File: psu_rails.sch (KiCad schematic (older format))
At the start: 16 parts, among them Q401 BC846BPN

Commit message: WIP: Assign footprints
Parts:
- C401, C402: footprint (none) -> Capacitor_SMD:C_1206_3216Metric_Pad1.42x1.75mm_HandSolder
- C403, C404: footprint (none) -> Capacitor_SMD:CP_Elec_8x10.5; Part number EEE1HA221UAP -> EEE1EA221UP
- C405, C406, C407, C408, C409: footprint (none) -> Capacitor_SMD:C_0603_1608Metric_Pad1.05x0.95mm_HandSolder
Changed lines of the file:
@@
 F 0 "C405" H 5300 3400 50  0000 L CNN
 F 1 "100n" H 5300 3300 50  0000 L CNN
-F 2 "" H 5388 2850 50  0001 C CNN
+F 2 "Capacitor_SMD:C_0603_1608Metric_Pad1.05x0.95mm_HandSolder" H 5388 2850 50  0001 C CNN
 F 3 "~" H 5350 3000 50  0001 C CNN
 F 4 "VJ0603Y104KXACW1BC" H 0   0   50  0001 C CNN "Part number"
@@
 F 0 "C407" H 5600 3400 50  0000 L CNN
 F 1 "100n" H 5600 3300 50  0000 L CNN
-F 2 "" H 5688 2850 50  0001 C CNN
+F 2 "Capacitor_SMD:C_0603_1608Metric_Pad1.05x0.95mm_HandSolder" H 5688 2850 50  0001 C CNN
 F 3 "~" H 5650 3000 50  0001 C CNN
 F 4 "VJ0603Y104KXACW1BC" H 0   0   50  0001 C CNN "Part number"
@@
 F 0 "C403" H 5000 3400 50  0000 L CNN
 F 1 "220u" H 4950 3300 50  0000 L CNN
-F 2 "" H 5088 2850 50  0001 C CNN
+F 2 "Capacitor_SMD:CP_Elec_8x10.5" H 5088 2850 50  0001 C CNN
 F 3 "~" H 5050 3000 50  0001 C CNN
-F 4 "EEE1HA221UAP" H 0   0   50  0001 C CNN "Part number"
+F 4 "EEE1EA221UP" H 0   0   50  0001 C CNN "Part number"
 F 5 "SMT Electrolytic 25V" H 0   0   50  0001 C CNN "Parameters"
 	1    5050 3000
@@
 AR Path="/5D8DB5B0/5D8DBE1B" Ref="#PWR0403"  Part="1"
 AR Path="/5D8E5F02/5D8DBE1B" Ref="#PWR0503"  Part="1"
-F 0 "#PWR0403" H 5050 2950 50  0001 C CNN
+F 0 "#PWR0503" H 5050 2950 50  0001 C CNN
 F 1 "GND" H 5055 3027 50  0000 C CNN
 F 2 "" H 5050 3200 50  0001 C CNN
@@
 AR Path="/5D8DB5B0/5D8DBE37" Ref="#PWR0405"  Part="1"
 AR Path="/5D8E5F02/5D8DBE37" Ref="#PWR0505"  Part="1"
-F 0 "#PWR0405" H 5350 2950 50  0001 C CNN
+F 0 "#PWR0505" H 5350 2950 50  0001 C CNN
 F 1 "GND" H 5355 3027 50  0000 C CNN
 F 2 "" H 5350 3200 50  0001 C CNN
@@
 AR Path="/5D8DB5B0/5D8DBE4C" Ref="#PWR0407"  Part="1"
 AR Path="/5D8E5F02/5D8DBE4C" Ref="#PWR0507"  Part="1"
-F 0 "#PWR0407" H 5650 2950 50  0001 C CNN
+F 0 "#PWR0507" H 5650 2950 50  0001 C CNN
 F 1 "GND" H 5655 3027 50  0000 C CNN
 F 2 "" H 5650 3200 50  0001 C CNN
@@
 AR Path="/5D8DB5B0/5D8DBF9B" Ref="#PWR0404"  Part="1"
 AR Path="/5D8E5F02/5D8DBF9B" Ref="#PWR0504"  Part="1"
-F 0 "#PWR0404" H 5050 4800 50  0001 C CNN
+F 0 "#PWR0504" H 5050 4800 50  0001 C CNN
 F 1 "GND" H 5055 4877 50  0000 C CNN
 F 2 "" H 5050 5050 50  0001 C CNN
@@
 AR Path="/5D8DB5B0/5D8DBFA1" Ref="#PWR0406"  Part="1"
 AR Path="/5D8E5F02/5D8DBFA1" Ref="#PWR0506"  Part="1"
-F 0 "#PWR0406" H 5350 4800 50  0001 C CNN
+F 0 "#PWR0506" H 5350 4800 50  0001 C CNN
 F 1 "GND" H 5355 4877 50  0000 C CNN
 F 2 "" H 5350 5050 50  0001 C CNN
@@
 AR Path="/5D8DB5B0/5D8DBFA7" Ref="#PWR0408"  Part="1"
 AR Path="/5D8E5F02/5D8DBFA7" Ref="#PWR0508"  Part="1"
-F 0 "#PWR0408" H 5650 4800 50  0001 C CNN
+F 0 "#PWR0508" H 5650 4800 50  0001 C CNN
 F 1 "GND" H 5655 4877 50  0000 C CNN
 F 2 "" H 5650 5050 50  0001 C CNN
@@
 F 0 "C409" H 6365 3796 50  0000 L CNN
 F 1 "100n" H 6365 3705 50  0000 L CNN
-F 2 "" H 6288 3600 50  0001 C CNN
+F 2 "Capacitor_SMD:C_0603_1608Metric_Pad1.05x0.95mm_HandSolder" H 6288 3600 50  0001 C CNN
 F 3 "~" H 6250 3750 50  0001 C CNN
 F 4 "VJ0603Y104KXACW1BC" H 0   0   50  0001 C CNN "Part number"
@@
 F 0 "C406" H 5300 5250 50  0000 L CNN
 F 1 "100n" H 5300 5150 50  0000 L CNN
-F 2 "" H 5388 4700 50  0001 C CNN
+F 2 "Capacitor_SMD:C_0603_1608Metric_Pad1.05x0.95mm_HandSolder" H 5388 4700 50  0001 C CNN
 F 3 "~" H 5350 4850 50  0001 C CNN
 F 4 "VJ0603Y104KXACW1BC" H 0   0   50  0001 C CNN "Part number"
@@
 F 0 "C408" H 5600 5250 50  0000 L CNN
 F 1 "100n" H 5600 5150 50  0000 L CNN
-F 2 "" H 5688 4700 50  0001 C CNN
+F 2 "Capacitor_SMD:C_0603_1608Metric_Pad1.05x0.95mm_HandSolder" H 5688 4700 50  0001 C CNN
 F 3 "~" H 5650 4850 50  0001 C CNN
 F 4 "VJ0603Y104KXACW1BC" H 0   0   50  0001 C CNN "Part number"
@@
 F 0 "C404" H 5000 4450 50  0000 L CNN
 F 1 "220u" H 4950 4550 50  0000 L CNN
-F 2 "" H 5088 4700 50  0001 C CNN
+F 2 "Capacitor_SMD:CP_Elec_8x10.5" H 5088 4700 50  0001 C CNN
 F 3 "~" H 5050 4850 50  0001 C CNN
-F 4 "EEE1HA221UAP" H 0   0   50  0001 C CNN "Part number"
+F 4 "EEE1EA221UP" H 0   0   50  0001 C CNN "Part number"
 F 5 "SMT Electrolytic 25V" H 0   0   50  0001 C CNN "Parameters"
 	1    5050 4850
@@
 F 0 "C401" H 4618 3696 50  0000 L CNN
 F 1 "10u" H 4618 3605 50  0000 L CNN
-F 2 "" H 4538 3500 50  0001 C CNN
+F 2 "Capacitor_SMD:C_1206_3216Metric_Pad1.42x1.75mm_HandSolder" H 4538 3500 50  0001 C CNN
 F 3 "~" H 4500 3650 50  0001 C CNN
 F 4 "X7R/X5R 25V 1206" H 0   0   50  0001 C CNN "Parameters"
@@
 F 0 "C402" H 4382 5454 50  0000 R CNN
 F 1 "10u" H 4382 5545 50  0000 R CNN
-F 2 "" H 4538 5350 50  0001 C CNN
+F 2 "Capacitor_SMD:C_1206_3216Metric_Pad1.42x1.75mm_HandSolder" H 4538 5350 50  0001 C CNN
 F 3 "~" H 4500 5500 50  0001 C CNN
 F 4 "X7R/X5R 25V 1206" H 0   0   50  0001 C CNN "Parameters"
@@
 AR Path="/5D8DB5B0/5D8DF531" Ref="#PWR0401"  Part="1"
 AR Path="/5D8E5F02/5D8DF531" Ref="#PWR0501"  Part="1"
-F 0 "#PWR0401" H 4500 3600 50  0001 C CNN
+F 0 "#PWR0501" H 4500 3600 50  0001 C CNN
 F 1 "GND" H 4505 3677 50  0000 C CNN
 F 2 "" H 4500 3850 50  0001 C CNN
@@
 AR Path="/5D8DB5B0/5D8DF556" Ref="#PWR0402"  Part="1"
 AR Path="/5D8E5F02/5D8DF556" Ref="#PWR0502"  Part="1"
-F 0 "#PWR0402" H 4500 5450 50  0001 C CNN
+F 0 "#PWR0502" H 4500 5450 50  0001 C CNN
 F 1 "GND" H 4505 5527 50  0000 C CNN
 F 2 "" H 4500 5700 50  0001 C CNN

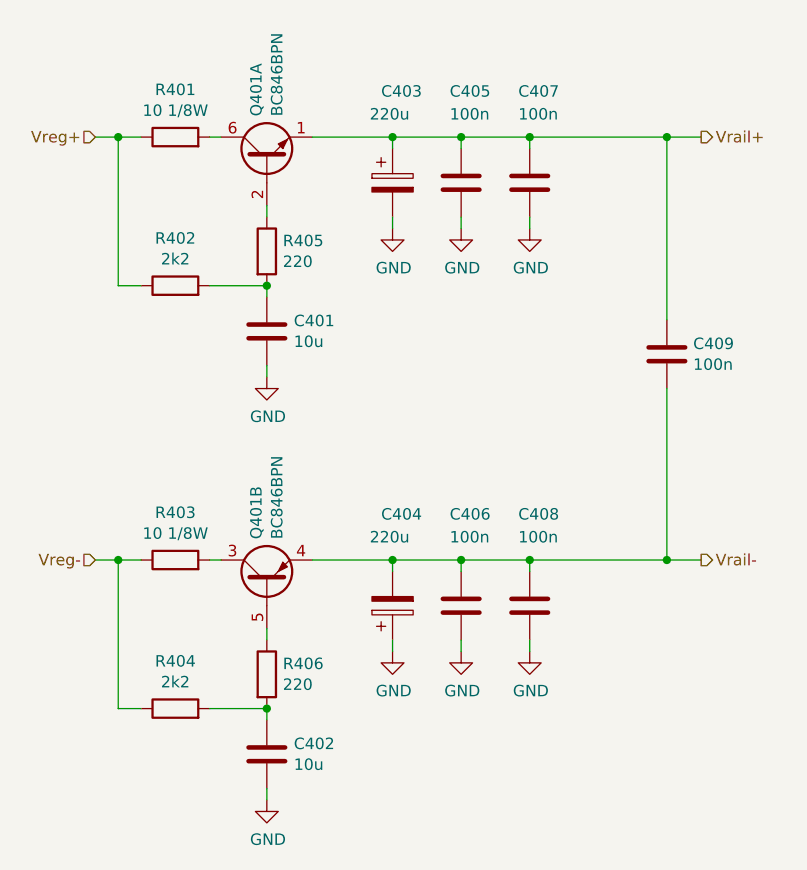
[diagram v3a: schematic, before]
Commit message: WIP: Assign footprints
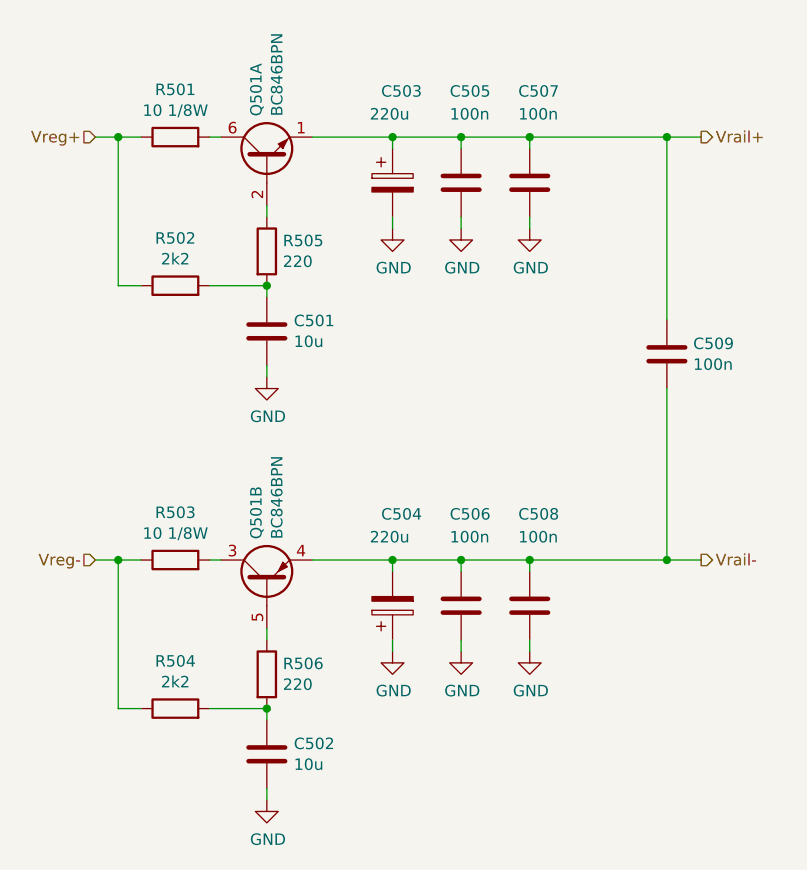
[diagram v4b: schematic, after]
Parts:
- R401, R403: footprint (none) -> Resistor_SMD:R_0805_2012Metric_Pad1.15x1.40mm_HandSolder
- R402, R404, R405, R406: footprint (none) -> Resistor_SMD:R_0603_1608Metric_Pad1.05x0.95mm_HandSolder
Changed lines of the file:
@@
 AR Path="/5D8DB5B0/5D8DB789" Ref="Q401"  Part="1"
 AR Path="/5D8E5F02/5D8DB789" Ref="Q501"  Part="1"
-F 0 "Q401" H 4691 2946 50  0000 L CNN
+F 0 "Q501" H 4691 2946 50  0000 L CNN
 F 1 "BC846BPN" H 4691 2855 50  0000 L CNN
 F 2 "Package_TO_SOT_SMD:SOT-363_SC-70-6" H 4700 3000 50  0001 C CNN
@@
 AR Path="/5D8DB5B0/5D8DB7C6" Ref="Q401"  Part="2"
 AR Path="/5D8E5F02/5D8DB7C6" Ref="Q501"  Part="2"
-F 0 "Q401" H 4691 4796 50  0000 L CNN
+F 0 "Q501" H 4691 4796 50  0000 L CNN
 F 1 "BC846BPN" H 4691 4705 50  0000 L CNN
 F 2 "Package_TO_SOT_SMD:SOT-363_SC-70-6" H 4700 4850 50  0001 C CNN
@@
 AR Path="/5D8DB5B0/5D8DBC14" Ref="C405"  Part="1"
 AR Path="/5D8E5F02/5D8DBC14" Ref="C505"  Part="1"
-F 0 "C405" H 5300 3400 50  0000 L CNN
+F 0 "C505" H 5300 3400 50  0000 L CNN
 F 1 "100n" H 5300 3300 50  0000 L CNN
 F 2 "Capacitor_SMD:C_0603_1608Metric_Pad1.05x0.95mm_HandSolder" H 5388 2850 50  0001 C CNN
@@
 AR Path="/5D8DB5B0/5D8DBC36" Ref="C407"  Part="1"
 AR Path="/5D8E5F02/5D8DBC36" Ref="C507"  Part="1"
-F 0 "C407" H 5600 3400 50  0000 L CNN
+F 0 "C507" H 5600 3400 50  0000 L CNN
 F 1 "100n" H 5600 3300 50  0000 L CNN
 F 2 "Capacitor_SMD:C_0603_1608Metric_Pad1.05x0.95mm_HandSolder" H 5688 2850 50  0001 C CNN
@@
 AR Path="/5D8DB5B0/5D8DBD04" Ref="C403"  Part="1"
 AR Path="/5D8E5F02/5D8DBD04" Ref="C503"  Part="1"
-F 0 "C403" H 5000 3400 50  0000 L CNN
+F 0 "C503" H 5000 3400 50  0000 L CNN
 F 1 "220u" H 4950 3300 50  0000 L CNN
 F 2 "Capacitor_SMD:CP_Elec_8x10.5" H 5088 2850 50  0001 C CNN
@@
 AR Path="/5D8DB5B0/5D8DC249" Ref="C409"  Part="1"
 AR Path="/5D8E5F02/5D8DC249" Ref="C509"  Part="1"
-F 0 "C409" H 6365 3796 50  0000 L CNN
+F 0 "C509" H 6365 3796 50  0000 L CNN
 F 1 "100n" H 6365 3705 50  0000 L CNN
 F 2 "Capacitor_SMD:C_0603_1608Metric_Pad1.05x0.95mm_HandSolder" H 6288 3600 50  0001 C CNN
@@
 AR Path="/5D8DB5B0/5D8DCC24" Ref="C406"  Part="1"
 AR Path="/5D8E5F02/5D8DCC24" Ref="C506"  Part="1"
-F 0 "C406" H 5300 5250 50  0000 L CNN
+F 0 "C506" H 5300 5250 50  0000 L CNN
 F 1 "100n" H 5300 5150 50  0000 L CNN
 F 2 "Capacitor_SMD:C_0603_1608Metric_Pad1.05x0.95mm_HandSolder" H 5388 4700 50  0001 C CNN
@@
 AR Path="/5D8DB5B0/5D8DCC2A" Ref="C408"  Part="1"
 AR Path="/5D8E5F02/5D8DCC2A" Ref="C508"  Part="1"
-F 0 "C408" H 5600 5250 50  0000 L CNN
+F 0 "C508" H 5600 5250 50  0000 L CNN
 F 1 "100n" H 5600 5150 50  0000 L CNN
 F 2 "Capacitor_SMD:C_0603_1608Metric_Pad1.05x0.95mm_HandSolder" H 5688 4700 50  0001 C CNN
@@
 AR Path="/5D8DB5B0/5D8DCC30" Ref="C404"  Part="1"
 AR Path="/5D8E5F02/5D8DCC30" Ref="C504"  Part="1"
-F 0 "C404" H 5000 4450 50  0000 L CNN
+F 0 "C504" H 5000 4450 50  0000 L CNN
 F 1 "220u" H 4950 4550 50  0000 L CNN
 F 2 "Capacitor_SMD:CP_Elec_8x10.5" H 5088 4700 50  0001 C CNN
@@
 AR Path="/5D8DB5B0/5D8DDC3C" Ref="C401"  Part="1"
 AR Path="/5D8E5F02/5D8DDC3C" Ref="C501"  Part="1"
-F 0 "C401" H 4618 3696 50  0000 L CNN
+F 0 "C501" H 4618 3696 50  0000 L CNN
 F 1 "10u" H 4618 3605 50  0000 L CNN
 F 2 "Capacitor_SMD:C_1206_3216Metric_Pad1.42x1.75mm_HandSolder" H 4538 3500 50  0001 C CNN
@@
 AR Path="/5D8DB5B0/5D8DE233" Ref="C402"  Part="1"
 AR Path="/5D8E5F02/5D8DE233" Ref="C502"  Part="1"
-F 0 "C402" H 4382 5454 50  0000 R CNN
+F 0 "C502" H 4382 5454 50  0000 R CNN
 F 1 "10u" H 4382 5545 50  0000 R CNN
 F 2 "Capacitor_SMD:C_1206_3216Metric_Pad1.42x1.75mm_HandSolder" H 4538 5350 50  0001 C CNN
@@
 AR Path="/5D8DB5B0/5D8DF470" Ref="R405"  Part="1"
 AR Path="/5D8E5F02/5D8DF470" Ref="R505"  Part="1"
-F 0 "R405" H 4570 3346 50  0000 L CNN
+F 0 "R505" H 4570 3346 50  0000 L CNN
 F 1 "220" H 4570 3255 50  0000 L CNN
-F 2 "" V 4430 3300 50  0001 C CNN
+F 2 "Resistor_SMD:R_0603_1608Metric_Pad1.05x0.95mm_HandSolder" V 4430 3300 50  0001 C CNN
 F 3 "~" H 4500 3300 50  0001 C CNN
 F 4 "ERA3AEB221V" H 0   0   50  0001 C CNN "Part number"
@@
 AR Path="/5D8DB5B0/5D8DF4B2" Ref="R406"  Part="1"
 AR Path="/5D8E5F02/5D8DF4B2" Ref="R506"  Part="1"
-F 0 "R406" H 4570 5196 50  0000 L CNN
+F 0 "R506" H 4570 5196 50  0000 L CNN
 F 1 "220" H 4570 5105 50  0000 L CNN
-F 2 "" V 4430 5150 50  0001 C CNN
+F 2 "Resistor_SMD:R_0603_1608Metric_Pad1.05x0.95mm_HandSolder" V 4430 5150 50  0001 C CNN
 F 3 "~" H 4500 5150 50  0001 C CNN
 F 4 "ERA3AEB221V" H 0   0   50  0001 C CNN "Part number"
@@
 AR Path="/5D8DB5B0/5D8E16D4" Ref="R401"  Part="1"
 AR Path="/5D8E5F02/5D8E16D4" Ref="R501"  Part="1"
-F 0 "R401" V 4307 2800 50  0000 C CNN
+F 0 "R501" V 4307 2800 50  0000 C CNN
 F 1 "10 1/8W" V 4216 2800 50  0000 C CNN
-F 2 "" V 4030 2800 50  0001 C CNN
+F 2 "Resistor_SMD:R_0805_2012Metric_Pad1.15x1.40mm_HandSolder" V 4030 2800 50  0001 C CNN
 F 3 "~" H 4100 2800 50  0001 C CNN
 F 4 "MCWF08U10RBTL" H 0   0   50  0001 C CNN "Part number"
@@
 AR Path="/5D8DB5B0/5D8E1F53" Ref="R402"  Part="1"
 AR Path="/5D8E5F02/5D8E1F53" Ref="R502"  Part="1"
-F 0 "R402" V 4307 3450 50  0000 C CNN
+F 0 "R502" V 4307 3450 50  0000 C CNN
 F 1 "2k2" V 4216 3450 50  0000 C CNN
-F 2 "" V 4030 3450 50  0001 C CNN
+F 2 "Resistor_SMD:R_0603_1608Metric_Pad1.05x0.95mm_HandSolder" V 4030 3450 50  0001 C CNN
 F 3 "~" H 4100 3450 50  0001 C CNN
 F 4 "RT0603FRE072K2L" H 0   0   50  0001 C CNN "Part number"
@@
 AR Path="/5D8DB5B0/5D8E1F97" Ref="R403"  Part="1"
 AR Path="/5D8E5F02/5D8E1F97" Ref="R503"  Part="1"
-F 0 "R403" V 4307 4650 50  0000 C CNN
+F 0 "R503" V 4307 4650 50  0000 C CNN
 F 1 "10 1/8W" V 4216 4650 50  0000 C CNN
-F 2 "" V 4030 4650 50  0001 C CNN
+F 2 "Resistor_SMD:R_0805_2012Metric_Pad1.15x1.40mm_HandSolder" V 4030 4650 50  0001 C CNN
 F 3 "~" H 4100 4650 50  0001 C CNN
 F 4 "MCWF08U10RBTL" H 0   0   50  0001 C CNN "Part number"
@@
 AR Path="/5D8DB5B0/5D8E1FEF" Ref="R404"  Part="1"
 AR Path="/5D8E5F02/5D8E1FEF" Ref="R504"  Part="1"
-F 0 "R404" V 4307 5300 50  0000 C CNN
+F 0 "R504" V 4307 5300 50  0000 C CNN
 F 1 "2k2" V 4216 5300 50  0000 C CNN
-F 2 "" V 4030 5300 50  0001 C CNN
+F 2 "Resistor_SMD:R_0603_1608Metric_Pad1.05x0.95mm_HandSolder" V 4030 5300 50  0001 C CNN
 F 3 "~" H 4100 5300 50  0001 C CNN
 F 4 "RT0603FRE072K2L" H 0   0   50  0001 C CNN "Part number"

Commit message: WIP: Assigning footprints
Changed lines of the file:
@@
 $Descr A4 11693 8268
 encoding utf-8
-Sheet 4 5
+Sheet 5 5
 Title ""
 Date ""
@@
 AR Path="/5D8DB5B0/5D8DB789" Ref="Q401"  Part="1"
 AR Path="/5D8E5F02/5D8DB789" Ref="Q501"  Part="1"
-F 0 "Q501" H 4691 2946 50  0000 L CNN
+F 0 "Q401" H 4691 2946 50  0000 L CNN
 F 1 "BC846BPN" H 4691 2855 50  0000 L CNN
 F 2 "Package_TO_SOT_SMD:SOT-363_SC-70-6" H 4700 3000 50  0001 C CNN
@@
 AR Path="/5D8DB5B0/5D8DB7C6" Ref="Q401"  Part="2"
 AR Path="/5D8E5F02/5D8DB7C6" Ref="Q501"  Part="2"
-F 0 "Q501" H 4691 4796 50  0000 L CNN
+F 0 "Q401" H 4691 4796 50  0000 L CNN
 F 1 "BC846BPN" H 4691 4705 50  0000 L CNN
 F 2 "Package_TO_SOT_SMD:SOT-363_SC-70-6" H 4700 4850 50  0001 C CNN
@@
 AR Path="/5D8DB5B0/5D8DBC14" Ref="C405"  Part="1"
 AR Path="/5D8E5F02/5D8DBC14" Ref="C505"  Part="1"
-F 0 "C505" H 5300 3400 50  0000 L CNN
+F 0 "C405" H 5300 3400 50  0000 L CNN
 F 1 "100n" H 5300 3300 50  0000 L CNN
 F 2 "Capacitor_SMD:C_0603_1608Metric_Pad1.05x0.95mm_HandSolder" H 5388 2850 50  0001 C CNN
@@
 AR Path="/5D8DB5B0/5D8DBC36" Ref="C407"  Part="1"
 AR Path="/5D8E5F02/5D8DBC36" Ref="C507"  Part="1"
-F 0 "C507" H 5600 3400 50  0000 L CNN
+F 0 "C407" H 5600 3400 50  0000 L CNN
 F 1 "100n" H 5600 3300 50  0000 L CNN
 F 2 "Capacitor_SMD:C_0603_1608Metric_Pad1.05x0.95mm_HandSolder" H 5688 2850 50  0001 C CNN
@@
 AR Path="/5D8DB5B0/5D8DBD04" Ref="C403"  Part="1"
 AR Path="/5D8E5F02/5D8DBD04" Ref="C503"  Part="1"
-F 0 "C503" H 5000 3400 50  0000 L CNN
+F 0 "C403" H 5000 3400 50  0000 L CNN
 F 1 "220u" H 4950 3300 50  0000 L CNN
 F 2 "Capacitor_SMD:CP_Elec_8x10.5" H 5088 2850 50  0001 C CNN
@@
 AR Path="/5D8DB5B0/5D8DC249" Ref="C409"  Part="1"
 AR Path="/5D8E5F02/5D8DC249" Ref="C509"  Part="1"
-F 0 "C509" H 6365 3796 50  0000 L CNN
+F 0 "C409" H 6365 3796 50  0000 L CNN
 F 1 "100n" H 6365 3705 50  0000 L CNN
 F 2 "Capacitor_SMD:C_0603_1608Metric_Pad1.05x0.95mm_HandSolder" H 6288 3600 50  0001 C CNN
@@
 AR Path="/5D8DB5B0/5D8DCC24" Ref="C406"  Part="1"
 AR Path="/5D8E5F02/5D8DCC24" Ref="C506"  Part="1"
-F 0 "C506" H 5300 5250 50  0000 L CNN
+F 0 "C406" H 5300 5250 50  0000 L CNN
 F 1 "100n" H 5300 5150 50  0000 L CNN
 F 2 "Capacitor_SMD:C_0603_1608Metric_Pad1.05x0.95mm_HandSolder" H 5388 4700 50  0001 C CNN
@@
 AR Path="/5D8DB5B0/5D8DCC2A" Ref="C408"  Part="1"
 AR Path="/5D8E5F02/5D8DCC2A" Ref="C508"  Part="1"
-F 0 "C508" H 5600 5250 50  0000 L CNN
+F 0 "C408" H 5600 5250 50  0000 L CNN
 F 1 "100n" H 5600 5150 50  0000 L CNN
 F 2 "Capacitor_SMD:C_0603_1608Metric_Pad1.05x0.95mm_HandSolder" H 5688 4700 50  0001 C CNN
@@
 AR Path="/5D8DB5B0/5D8DCC30" Ref="C404"  Part="1"
 AR Path="/5D8E5F02/5D8DCC30" Ref="C504"  Part="1"
-F 0 "C504" H 5000 4450 50  0000 L CNN
+F 0 "C404" H 5000 4450 50  0000 L CNN
 F 1 "220u" H 4950 4550 50  0000 L CNN
 F 2 "Capacitor_SMD:CP_Elec_8x10.5" H 5088 4700 50  0001 C CNN
@@
 AR Path="/5D8DB5B0/5D8DDC3C" Ref="C401"  Part="1"
 AR Path="/5D8E5F02/5D8DDC3C" Ref="C501"  Part="1"
-F 0 "C501" H 4618 3696 50  0000 L CNN
+F 0 "C401" H 4618 3696 50  0000 L CNN
 F 1 "10u" H 4618 3605 50  0000 L CNN
 F 2 "Capacitor_SMD:C_1206_3216Metric_Pad1.42x1.75mm_HandSolder" H 4538 3500 50  0001 C CNN
@@
 AR Path="/5D8DB5B0/5D8DE233" Ref="C402"  Part="1"
 AR Path="/5D8E5F02/5D8DE233" Ref="C502"  Part="1"
-F 0 "C502" H 4382 5454 50  0000 R CNN
+F 0 "C402" H 4382 5454 50  0000 R CNN
 F 1 "10u" H 4382 5545 50  0000 R CNN
 F 2 "Capacitor_SMD:C_1206_3216Metric_Pad1.42x1.75mm_HandSolder" H 4538 5350 50  0001 C CNN
@@
 AR Path="/5D8DB5B0/5D8DF470" Ref="R405"  Part="1"
 AR Path="/5D8E5F02/5D8DF470" Ref="R505"  Part="1"
-F 0 "R505" H 4570 3346 50  0000 L CNN
+F 0 "R405" H 4570 3346 50  0000 L CNN
 F 1 "220" H 4570 3255 50  0000 L CNN
 F 2 "Resistor_SMD:R_0603_1608Metric_Pad1.05x0.95mm_HandSolder" V 4430 3300 50  0001 C CNN
@@
 AR Path="/5D8DB5B0/5D8DF4B2" Ref="R406"  Part="1"
 AR Path="/5D8E5F02/5D8DF4B2" Ref="R506"  Part="1"
-F 0 "R506" H 4570 5196 50  0000 L CNN
+F 0 "R406" H 4570 5196 50  0000 L CNN
 F 1 "220" H 4570 5105 50  0000 L CNN
 F 2 "Resistor_SMD:R_0603_1608Metric_Pad1.05x0.95mm_HandSolder" V 4430 5150 50  0001 C CNN
@@
 AR Path="/5D8DB5B0/5D8E16D4" Ref="R401"  Part="1"
 AR Path="/5D8E5F02/5D8E16D4" Ref="R501"  Part="1"
-F 0 "R501" V 4307 2800 50  0000 C CNN
+F 0 "R401" V 4307 2800 50  0000 C CNN
 F 1 "10 1/8W" V 4216 2800 50  0000 C CNN
 F 2 "Resistor_SMD:R_0805_2012Metric_Pad1.15x1.40mm_HandSolder" V 4030 2800 50  0001 C CNN
@@
 AR Path="/5D8DB5B0/5D8E1F53" Ref="R402"  Part="1"
 AR Path="/5D8E5F02/5D8E1F53" Ref="R502"  Part="1"
-F 0 "R502" V 4307 3450 50  0000 C CNN
+F 0 "R402" V 4307 3450 50  0000 C CNN
 F 1 "2k2" V 4216 3450 50  0000 C CNN
 F 2 "Resistor_SMD:R_0603_1608Metric_Pad1.05x0.95mm_HandSolder" V 4030 3450 50  0001 C CNN
@@
 AR Path="/5D8DB5B0/5D8E1F97" Ref="R403"  Part="1"
 AR Path="/5D8E5F02/5D8E1F97" Ref="R503"  Part="1"
-F 0 "R503" V 4307 4650 50  0000 C CNN
+F 0 "R403" V 4307 4650 50  0000 C CNN
 F 1 "10 1/8W" V 4216 4650 50  0000 C CNN
 F 2 "Resistor_SMD:R_0805_2012Metric_Pad1.15x1.40mm_HandSolder" V 4030 4650 50  0001 C CNN
@@
 AR Path="/5D8DB5B0/5D8E1FEF" Ref="R404"  Part="1"
 AR Path="/5D8E5F02/5D8E1FEF" Ref="R504"  Part="1"
-F 0 "R504" V 4307 5300 50  0000 C CNN
+F 0 "R404" V 4307 5300 50  0000 C CNN
 F 1 "2k2" V 4216 5300 50  0000 C CNN
 F 2 "Resistor_SMD:R_0603_1608Metric_Pad1.05x0.95mm_HandSolder" V 4030 5300 50  0001 C CNN
